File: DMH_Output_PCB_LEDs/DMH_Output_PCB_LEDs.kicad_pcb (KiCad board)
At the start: 2 copper layers, 37.5 x 81 mm, 4 parts, among them J0 Conn_01x01

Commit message: Generated Gerbers for prototyping
Panel, Controls and LEDs only
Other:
- board text added: "Mk1.0 - March 2026"
- board text removed: "Mk1.0 - Month Year"
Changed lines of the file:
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@@
 			(plot_on_all_layers_selection 0x00000000_00000000_00000000_00000000)
 			(disableapertmacros no)
-			(usegerberextensions no)
+			(usegerberextensions yes)
 			(usegerberattributes yes)
 			(usegerberadvancedattributes yes)
@@
 			(sketchdnponfab yes)
 			(crossoutdnponfab yes)
-			(subtractmaskfromsilk no)
+			(subtractmaskfromsilk yes)
 			(outputformat 1)
 			(mirror no)
-			(drillshape 1)
+			(drillshape 0)
 			(scaleselection 1)
-			(outputdirectory "")
+			(outputdirectory "Gerbers/")
 		)
 	)
@@
 		(layer "User.9")
 	)
-	(gr_text "Mk1.0 - Month Year"
-		(at 78.75 147.5 90)
+	(gr_text "Mk1.0 - March 2026"
+		(at 78.75 144.75 90)
 		(layer "B.SilkS")
 		(effects

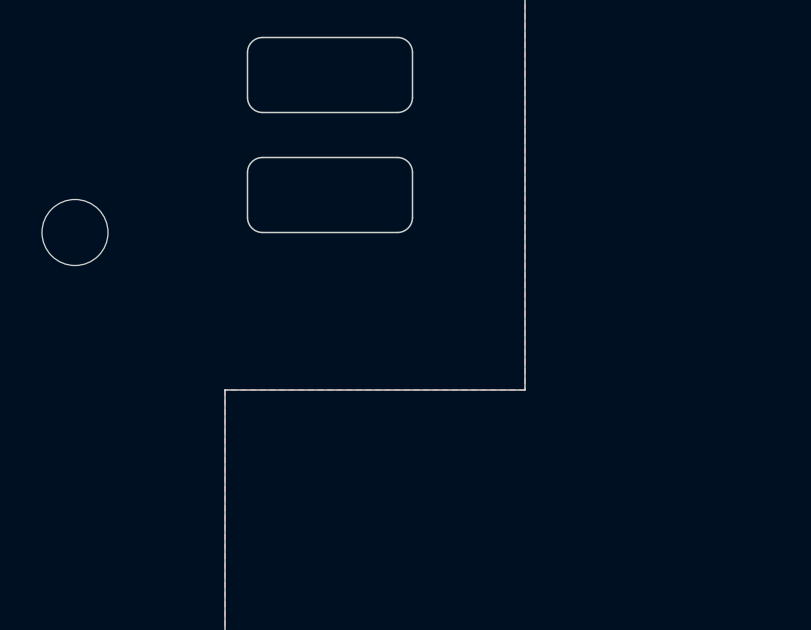
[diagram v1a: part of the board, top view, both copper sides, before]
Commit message: Regenerated LEDs baffle Gerbers
Added second GND plated hole to avoid issues with the probe test at JLC
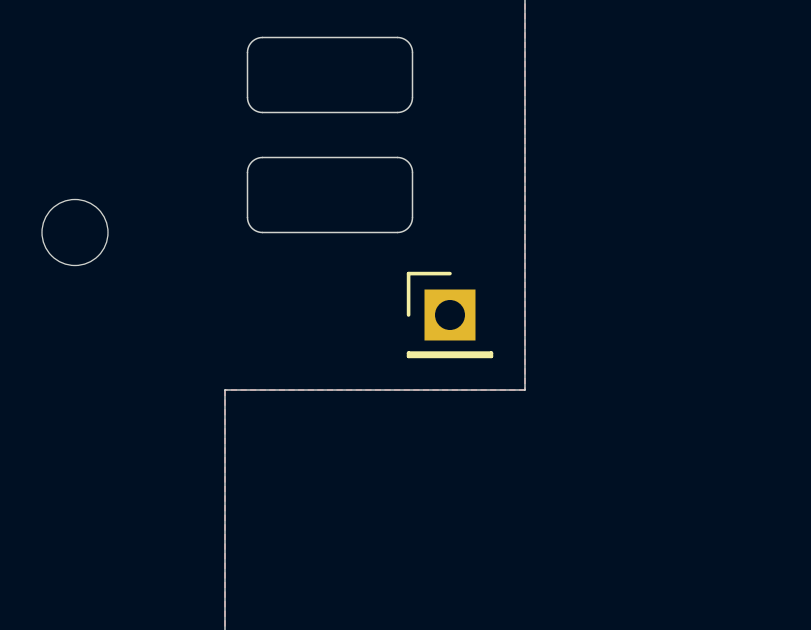
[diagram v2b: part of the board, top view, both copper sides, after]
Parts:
- added J29: Conn_01x01, Connector_PinHeader_2.54mm:PinHeader_1x01_P2.54mm_Vertical, F.Cu at (87.5, 130.0)
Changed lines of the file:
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@@
 	(net 0 "")
 	(net 1 "GND")
+	(footprint "Connector_PinHeader_2.54mm:PinHeader_1x01_P2.54mm_Vertical"
+		(layer "F.Cu")
+		(at 87.5 130)
+		(descr "Through hole straight pin header, 1x01, 2.54mm pitch, single row")
+		(tags "Through hole pin header THT 1x01 2.54mm single row")
+		(property "Reference" "J29"
+			(at 0 -2.38 0)
+			(layer "F.SilkS")
+			(hide yes)
+			(effects
+				(font
+					(size 1 1)
+					(thickness 0.15)
+				)
+			)
+		)
+		(property "Value" "Conn_01x01"
+			(at 0 2.38 0)
+			(layer "F.Fab")
+			(hide yes)
+			(effects
+				(font
+					(size 1 1)
+					(thickness 0.15)
+				)
+			)
+		)
+		(property "Datasheet" "~"
+			(at 0 0 0)
+			(layer "F.Fab")
+			(hide yes)
+			(effects
+				(font
+					(size 1.27 1.27)
+					(thickness 0.15)
+				)
+			)
+		)
+		(property "Description" "Generic connector, single row, 01x01, script generated (kicad-library-utils/schlib/autogen/connector/)"
+			(at 0 0 0)
+			(layer "F.Fab")
+			(hide yes)
+			(effects
+				(font
+					(size 1.27 1.27)
+					(thickness 0.15)
+				)
+			)
+		)
+		(property "Function" "Panel GND"
+			(at 0 0 0)
+			(unlocked yes)
+			(layer "F.Fab")
+			(hide yes)
+			(effects
+				(font
+					(size 1 1)
+					(thickness 0.15)
+				)
+			)
+		)
+		(property ki_fp_filters "Connector*:*_1x??_*")
+		(sheetname "/Power/")
+		(sheetfile "Power.kicad_sch")
+		(attr through_hole exclude_from_bom dnp)
+		(fp_line
+			(start -1.38 -1.38)
+			(end 0 -1.38)
+			(stroke
+				(width 0.12)
+				(type solid)
+			)
+			(layer "F.SilkS")
+		)
+		(fp_line
+			(start -1.38 0)
+			(end -1.38 -1.38)
+			(stroke
+				(width 0.12)
+				(type solid)
+			)
+			(layer "F.SilkS")
+		)
+		(fp_line
+			(start -1.38 1.27)
+			(end -1.38 1.38)
+			(stroke
+				(width 0.12)
+				(type solid)
+			)
+			(layer "F.SilkS")
+		)
+		(fp_line
+			(start -1.38 1.27)
+			(end 1.38 1.27)
+			(stroke
+				(width 0.12)
+				(type solid)
+			)
+			(layer "F.SilkS")
+		)
+		(fp_line
+			(start -1.38 1.38)
+			(end 1.38 1.38)
+			(stroke
+				(width 0.12)
+				(type solid)
+			)
+			(layer "F.SilkS")
+		)
+		(fp_line
+			(start 1.38 1.27)
+			(end 1.38 1.38)
+			(stroke
+				(width 0.12)
+				(type solid)
+			)
+			(layer "F.SilkS")
+		)
+		(fp_rect
+			(start -1.77 -1.77)
+			(end 1.77 1.77)
+			(stroke
+				(width 0.05)
+				(type solid)
+			)
+			(fill no)
+			(layer "F.CrtYd")
+		)
+		(fp_line
+			(start -1.27 -0.635)
+			(end -0.635 -1.27)
+			(stroke
+				(width 0.1)
+				(type solid)
+			)
+			(layer "F.Fab")
+		)
+		(fp_line
+			(start -1.27 1.27)
+			(end -1.27 -0.635)
+			(stroke
+				(width 0.1)
+				(type solid)
+			)
+			(layer "F.Fab")
+		)
+		(fp_line
+			(start -0.635 -1.27)
+			(end 1.27 -1.27)
+			(stroke
+				(width 0.1)
+				(type solid)
+			)
+			(layer "F.Fab")
+		)
+		(fp_line
+			(start 1.27 -1.27)
+			(end 1.27 1.27)
+			(stroke
+				(width 0.1)
+				(type solid)
+			)
+			(layer "F.Fab")
+		)
+		(fp_line
+			(start 1.27 1.27)
+			(end -1.27 1.27)
+			(stroke
+				(width 0.1)
+				(type solid)
+			)
+			(layer "F.Fab")
+		)
+		(pad "1" thru_hole rect
+			(at 0 0)
+			(size 1.7 1.7)
+			(drill 1)
+			(layers "*.Cu" "*.Mask")
+			(remove_unused_layers no)
+			(net 1 "GND")
+			(pinfunction "Pin_1")
+			(pintype "passive")
+		)
+		(embedded_fonts no)
+		(model "${KICAD9_3DMODEL_DIR}/Connector_PinHeader_2.54mm.3dshapes/PinHeader_1x01_P2.54mm_Vertical.step"
+			(offset
+				(xyz 0 0 0)
+			)
+			(scale
+				(xyz 1 1 1)
+			)
+			(rotate
+				(xyz 0 0 0)
+			)
+		)
+	)
 	(footprint "MountingHole:MountingHole_2.2mm_M2"
 		(layer "F.Cu")

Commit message: Re-exported all Gerbers
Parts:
- removed H23: MountingHole, MountingHole:MountingHole_2.2mm_M2
- H21, H22: footprint MountingHole:MountingHole_2.2mm_M2 -> MountingHole:MountingHole_2.7mm_M2.5_ISO14580
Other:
- board text added: "Mk1.1 - June 2026"
- board text removed: "Mk1.0 - March 2026"
